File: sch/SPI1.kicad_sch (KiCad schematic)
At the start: 12 parts, among them U6 BMP581, U7 MMC5983MA, U8 ADXL375, U9 LSM6DSV16X

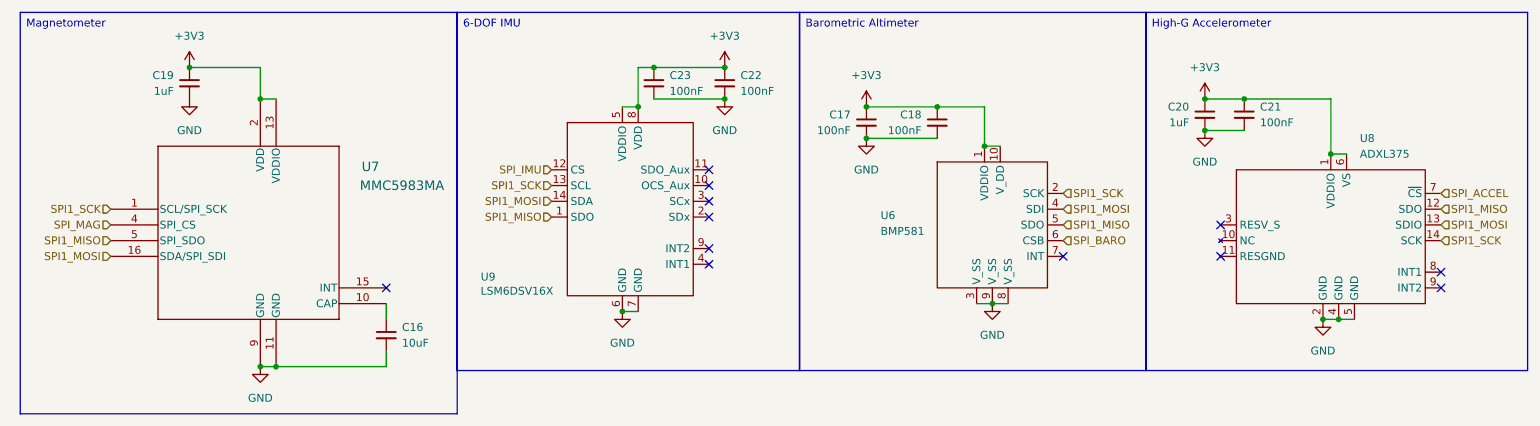
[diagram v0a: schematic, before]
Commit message: schematic update
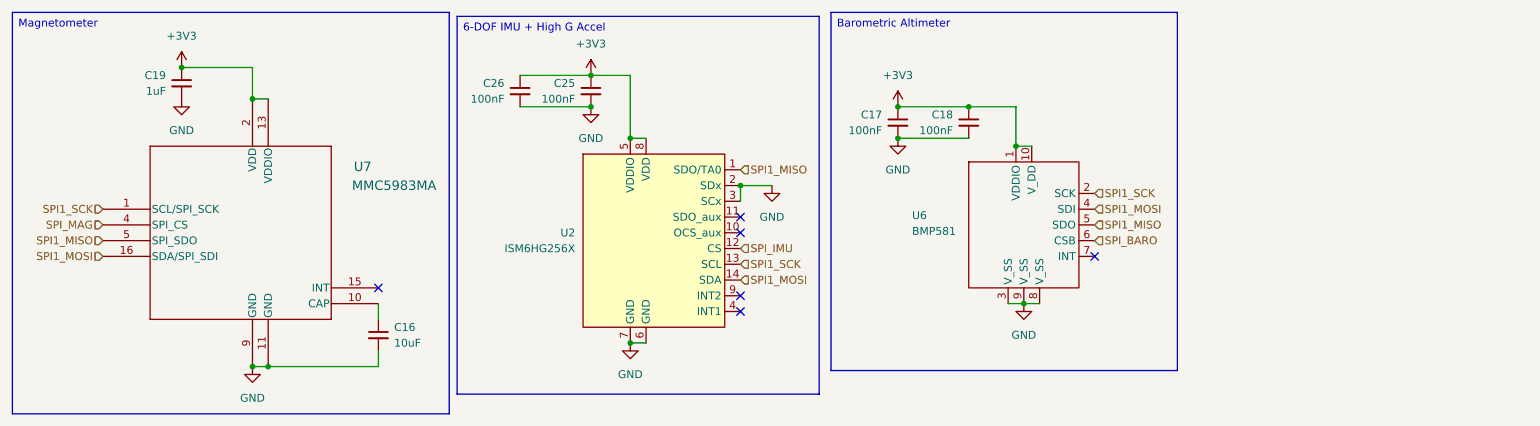
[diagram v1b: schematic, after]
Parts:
- removed C20: 1uF, Capacitor_SMD:C_0402_1005Metric, symbol Device:C_Small
- removed C21, C22, C23: 100nF, Capacitor_SMD:C_0402_1005Metric, symbol Device:C_Small
- removed U8: ADXL375, Package_LGA:LGA-14_3x5mm_P0.8mm_LayoutBorder1x6y, symbol Sensors:ADXL375
- removed U9: LSM6DSV16X, LSM6DSV16X:LGA-14L_STM-L, symbol Sensors:LSM6DSV16X
- added C25, C26: 100nF, Capacitor_SMD:C_0402_1005Metric, symbol Device:C_Small
- added U2: ISM6HG256X, ISM6HG256XTR:LGA14L_2P5X3_STM, symbol ISM6HG256X:ISM6HG256X
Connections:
- net +3V3: now also C25.1, C26.1, U2.5 (VDDIO), U2.8 (VDD)
- net GND: now also C25.2, C26.2, U2.2 (SDx), U2.3 (SCx), U2.6 (GND), U2.7 (GND)
- net SPI1_MISO: now also U2.1 (SDO/TA0)
- net SPI1_MOSI: now also U2.14 (SDA)
- net SPI1_SCK: now also U2.13 (SCL)
- net SPI_IMU: now also U2.12 (CS)
- no-connect marks 12 -> 6
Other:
- moved on the sheet: C16, C17, C18, C19, U6, U7
